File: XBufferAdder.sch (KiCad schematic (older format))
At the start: 8 parts, among them U11 NE5532

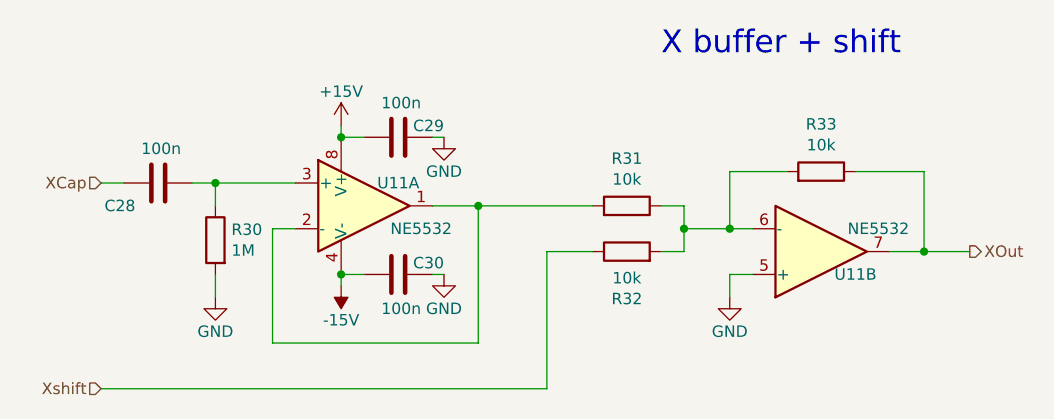
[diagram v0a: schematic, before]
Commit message: Fixed some bugs, finished block symbols
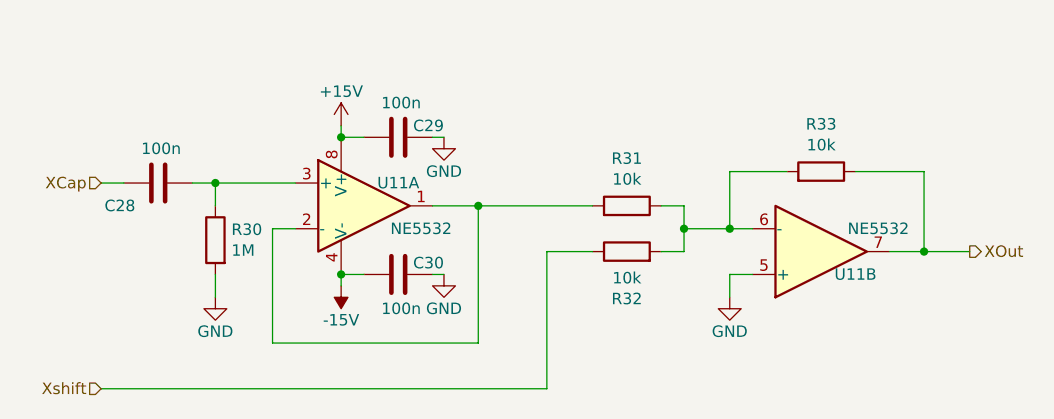
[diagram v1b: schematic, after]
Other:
- note removed: "X buffer + shift"
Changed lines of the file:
@@
 encoding utf-8
 Sheet 10 13
-Title ""
-Date ""
-Rev ""
-Comp ""
-Comment1 ""
+Title "X Buffer/Adder"
+Date "2021-04-20"
+Rev "2.0"
+Comp "Filip Piórski"
+Comment1 "Buffers the X signal and adds an offset (shift)"
 Comment2 ""
 Comment3 ""
@@
 	7000 4150 7200 4150
 Connection ~ 7000 4150
-Text Notes 5850 3300 0    100  ~ 0
-X buffer + shift
 Wire Wire Line
 	5350 4150 5350 4750
